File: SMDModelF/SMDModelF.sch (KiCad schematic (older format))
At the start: 44 parts, among them J1 Model F Ribbon Cable, J2 PadsToShort, J3 EXPANSION HEADER, J5 Conn_01x03, J7 Conn_01x05, U1 MCP4921-E, U2 LM339A, U3 74AHC595, U4 74AHC595, U5 ProMicro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

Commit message: Added footprints for no-3d solenoid header, and with 3d for beeper header
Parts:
- J7: footprint Connector_PinHeader_2.54mm:PinHeader_1x05_P2.54mm_Vertical -> TH-XWhatsIt:PinHeader_1x05_P2.54mm_Vertical_no3d
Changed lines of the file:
@@
 F 0 "J7" H 7468 5775 50  0000 C CNN
 F 1 "Conn_01x05" H 7468 5866 50  0000 C CNN
-F 2 "Connector_PinHeader_2.54mm:PinHeader_1x05_P2.54mm_Vertical" H 7550 6200 50  0001 C CNN
+F 2 "TH-XWhatsIt:PinHeader_1x05_P2.54mm_Vertical_no3d" H 7550 6200 50  0001 C CNN
 F 3 "~" H 7550 6200 50  0001 C CNN
 	1    7550 6200

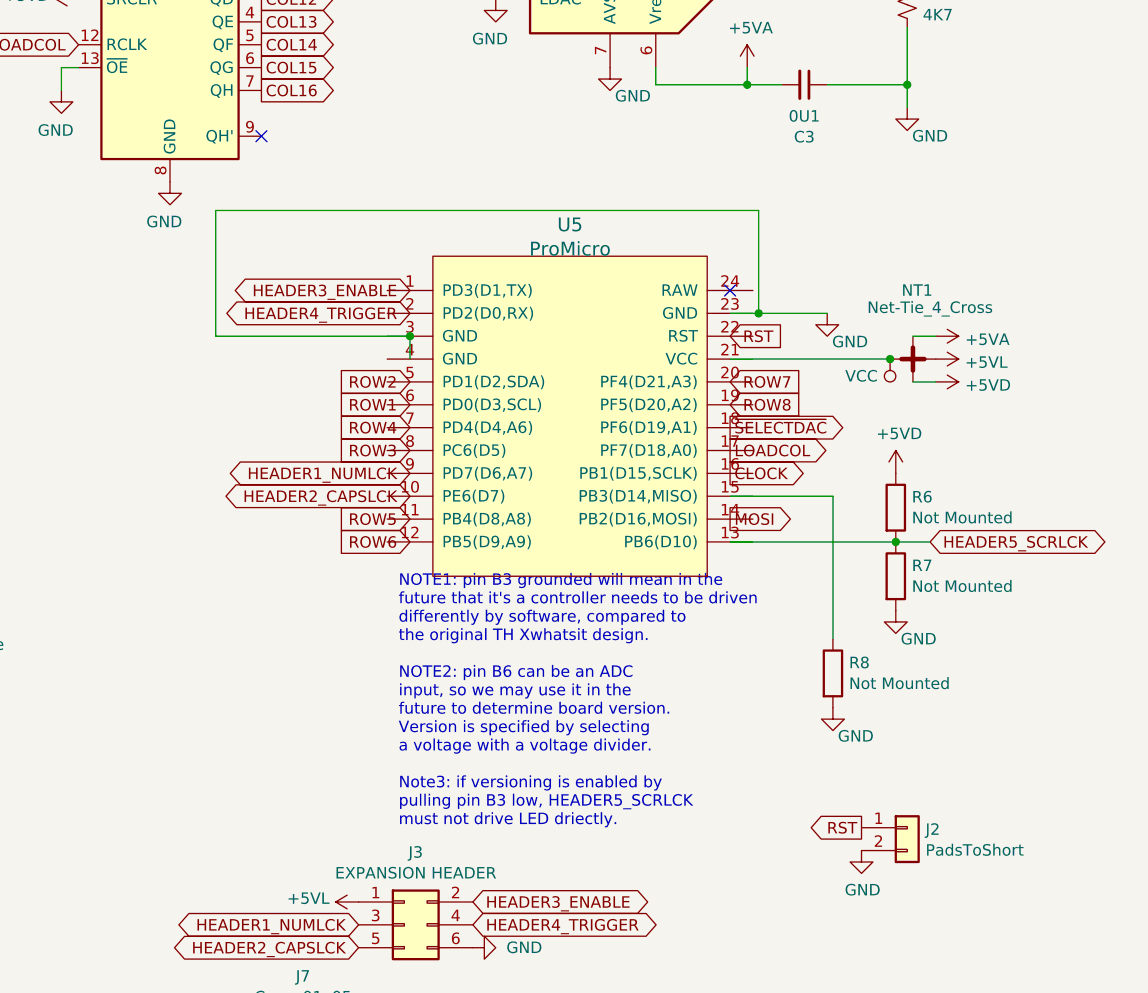
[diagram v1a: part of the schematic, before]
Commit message: Updated pro micro schematic symbol, and added PDF schematics
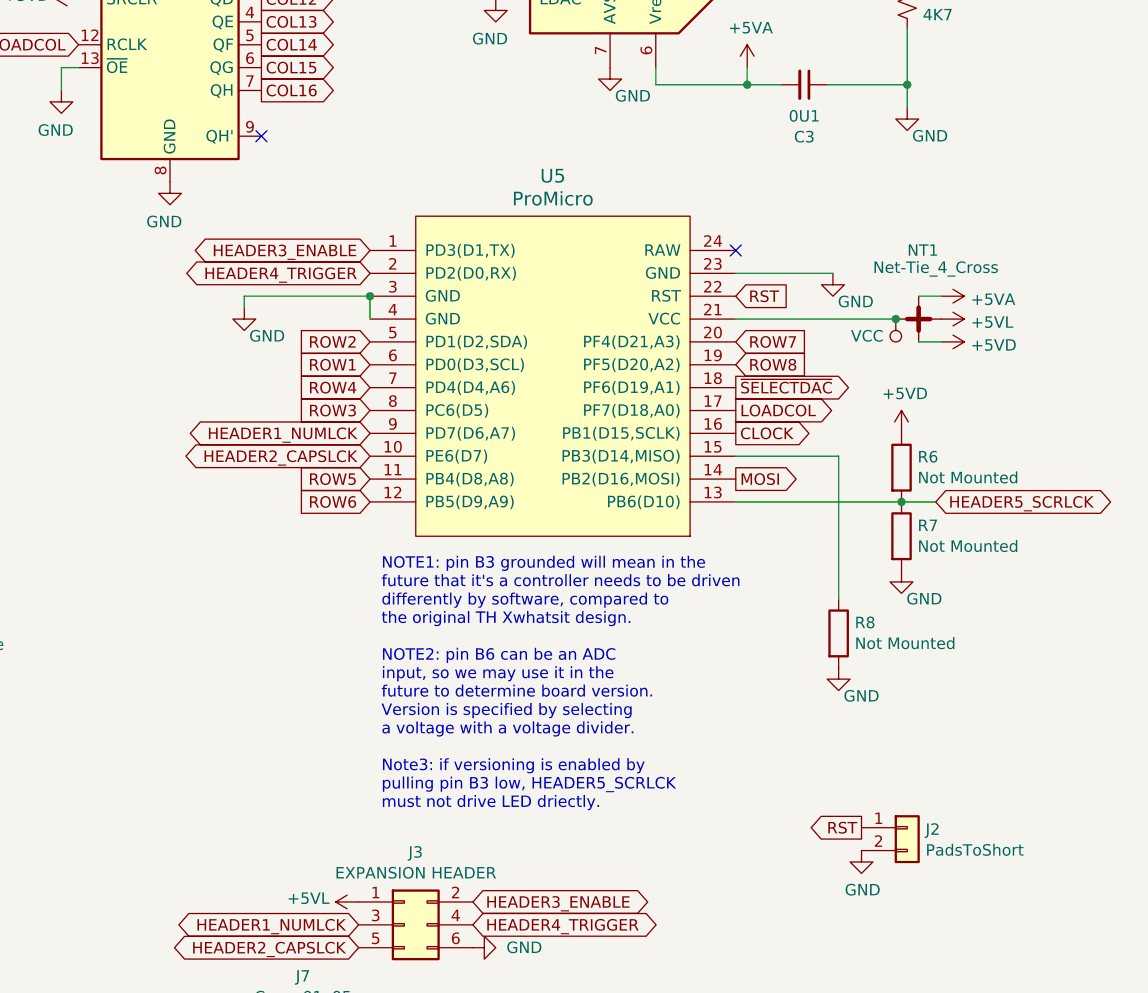
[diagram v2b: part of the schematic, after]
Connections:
- wire segments 98 -> 95
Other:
- moved on the sheet: NT1, R6, R7, R8, U5

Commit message: Updated 100k resistor and shift register LCSC part numbers
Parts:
- R10, R11, R12, R13, R14, R15, R16, R9: LCSC C17407 -> C149504
- U3, U4: LCSC C5520 -> C2682116
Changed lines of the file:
@@
 F 2 "Package_SO:SOIC-16_3.9x9.9mm_P1.27mm" H 5275 1575 50  0001 C CNN
 F 3 "https://assets.nexperia.com/documents/data-sheet/74HC_HCT595.pdf" H 5275 1575 50  0001 C CNN
-F 4 "C5520" H 5275 1575 50  0001 C CNN "LCSC"
+F 4 "C2682116" H 5275 1575 50  0001 C CNN "LCSC"
 	1    5275 1575
 	1    0    0    -1
@@
 F 2 "Package_SO:SOIC-16_3.9x9.9mm_P1.27mm" H 7050 1600 50  0001 C CNN
 F 3 "https://assets.nexperia.com/documents/data-sheet/74HC_HCT595.pdf" H 7050 1600 50  0001 C CNN
-F 4 "C5520" H 7050 1600 50  0001 C CNN "LCSC"
+F 4 "C2682116" H 7050 1600 50  0001 C CNN "LCSC"
 	1    7050 1600
 	1    0    0    -1
@@
 F 2 "Resistor_SMD:R_0805_2012Metric_Pad1.15x1.40mm_HandSolder" V 1380 1325 50  0001 C CNN
 F 3 "~" H 1450 1325 50  0001 C CNN
-F 4 "C17407" H 1450 1325 50  0001 C CNN "LCSC"
+F 4 "C149504" H 1450 1325 50  0001 C CNN "LCSC"
 	1    1450 1325
 	1    0    0    -1
@@
 F 2 "Resistor_SMD:R_0805_2012Metric_Pad1.15x1.40mm_HandSolder" V 1380 1925 50  0001 C CNN
 F 3 "~" H 1450 1925 50  0001 C CNN
-F 4 "C17407" H 1450 1925 50  0001 C CNN "LCSC"
+F 4 "C149504" H 1450 1925 50  0001 C CNN "LCSC"
 	1    1450 1925
 	1    0    0    -1
@@
 F 2 "Resistor_SMD:R_0805_2012Metric_Pad1.15x1.40mm_HandSolder" V 1380 2525 50  0001 C CNN
 F 3 "~" H 1450 2525 50  0001 C CNN
-F 4 "C17407" H 1450 2525 50  0001 C CNN "LCSC"
+F 4 "C149504" H 1450 2525 50  0001 C CNN "LCSC"
 	1    1450 2525
 	1    0    0    -1
@@
 F 2 "Resistor_SMD:R_0805_2012Metric_Pad1.15x1.40mm_HandSolder" V 1380 3125 50  0001 C CNN
 F 3 "~" H 1450 3125 50  0001 C CNN
-F 4 "C17407" H 1450 3125 50  0001 C CNN "LCSC"
+F 4 "C149504" H 1450 3125 50  0001 C CNN "LCSC"
 	1    1450 3125
 	1    0    0    -1
@@
 F 2 "Resistor_SMD:R_0805_2012Metric_Pad1.15x1.40mm_HandSolder" V 1380 4050 50  0001 C CNN
 F 3 "~" H 1450 4050 50  0001 C CNN
-F 4 "C17407" H 1450 4050 50  0001 C CNN "LCSC"
+F 4 "C149504" H 1450 4050 50  0001 C CNN "LCSC"
 	1    1450 4050
 	1    0    0    -1
@@
 F 2 "Resistor_SMD:R_0805_2012Metric_Pad1.15x1.40mm_HandSolder" V 1380 4650 50  0001 C CNN
 F 3 "~" H 1450 4650 50  0001 C CNN
-F 4 "C17407" H 1450 4650 50  0001 C CNN "LCSC"
+F 4 "C149504" H 1450 4650 50  0001 C CNN "LCSC"
 	1    1450 4650
 	1    0    0    -1
@@
 F 2 "Resistor_SMD:R_0805_2012Metric_Pad1.15x1.40mm_HandSolder" V 1380 5250 50  0001 C CNN
 F 3 "~" H 1450 5250 50  0001 C CNN
-F 4 "C17407" H 1450 5250 50  0001 C CNN "LCSC"
+F 4 "C149504" H 1450 5250 50  0001 C CNN "LCSC"
 	1    1450 5250
 	1    0    0    -1
@@
 F 2 "Resistor_SMD:R_0805_2012Metric_Pad1.15x1.40mm_HandSolder" V 1380 5850 50  0001 C CNN
 F 3 "~" H 1450 5850 50  0001 C CNN
-F 4 "C17407" H 1450 5850 50  0001 C CNN "LCSC"
+F 4 "C149504" H 1450 5850 50  0001 C CNN "LCSC"
 	1    1450 5850
 	1    0    0    -1

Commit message: Revert part of commit 'Updated 100k resistor and shift register LCSC part numbers' (the shift register BOM changes only)
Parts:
- U3, U4: LCSC C2682116 -> C5520
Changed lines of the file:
@@
 F 2 "Package_SO:SOIC-16_3.9x9.9mm_P1.27mm" H 5275 1575 50  0001 C CNN
 F 3 "https://assets.nexperia.com/documents/data-sheet/74HC_HCT595.pdf" H 5275 1575 50  0001 C CNN
-F 4 "C2682116" H 5275 1575 50  0001 C CNN "LCSC"
+F 4 "C5520" H 5275 1575 50  0001 C CNN "LCSC"
 	1    5275 1575
 	1    0    0    -1
@@
 F 2 "Package_SO:SOIC-16_3.9x9.9mm_P1.27mm" H 7050 1600 50  0001 C CNN
 F 3 "https://assets.nexperia.com/documents/data-sheet/74HC_HCT595.pdf" H 7050 1600 50  0001 C CNN
-F 4 "C2682116" H 7050 1600 50  0001 C CNN "LCSC"
+F 4 "C5520" H 7050 1600 50  0001 C CNN "LCSC"
 	1    7050 1600
 	1    0    0    -1
